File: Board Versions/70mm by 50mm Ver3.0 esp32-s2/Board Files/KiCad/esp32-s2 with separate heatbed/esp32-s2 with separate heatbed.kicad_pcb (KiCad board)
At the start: 2 copper layers, 65.5 x 50 mm, 58 parts, among them IC1 ESP32-S2FN4R2, J1 PJ-037B, J2 USB4520-03-0-A, J3 TB003-500-P02BE, J4 TB003-500-P02BE, J5 Conn_01x03_Male, Q1 PJD25N06A_L2_00001, U1 LD1117S33TR_SOT223, U2 MAX31855KASA, Y1 ECS-400-15-33B-CTN-TR

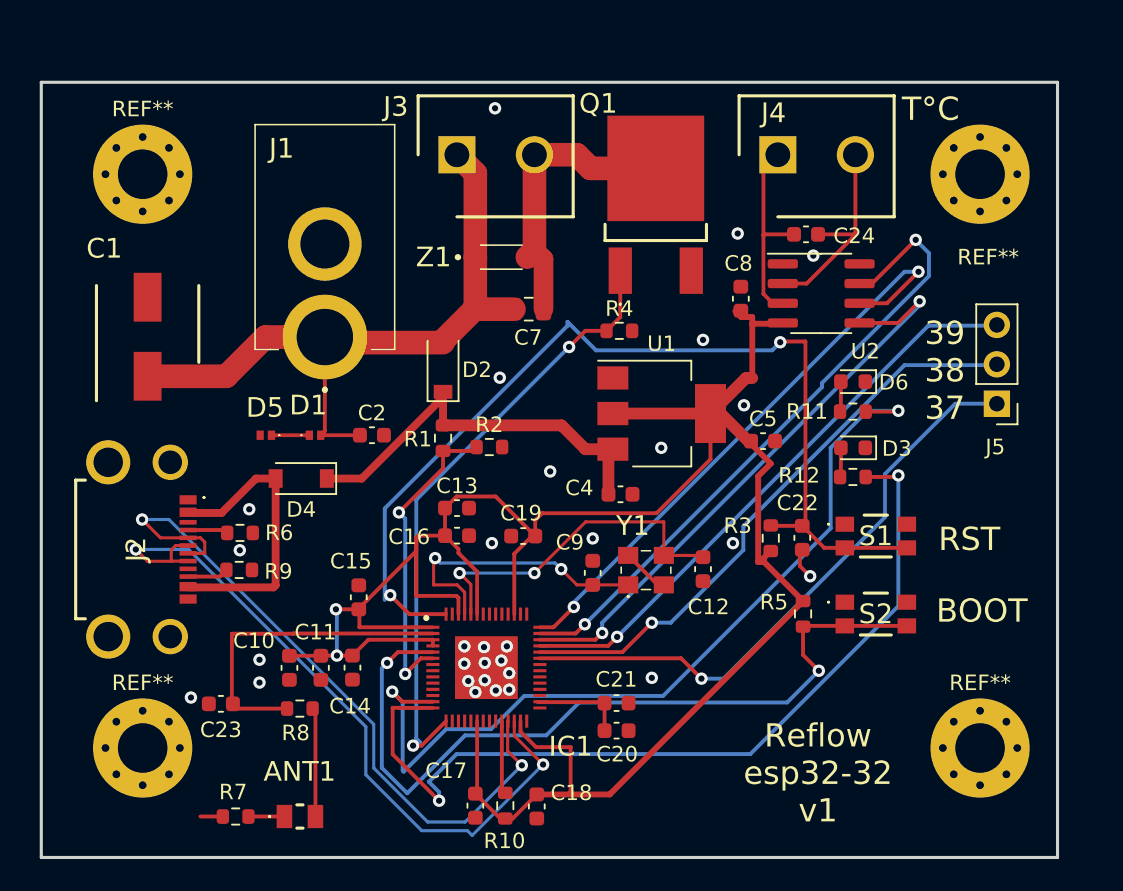
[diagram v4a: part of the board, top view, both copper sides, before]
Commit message: New mounting holes
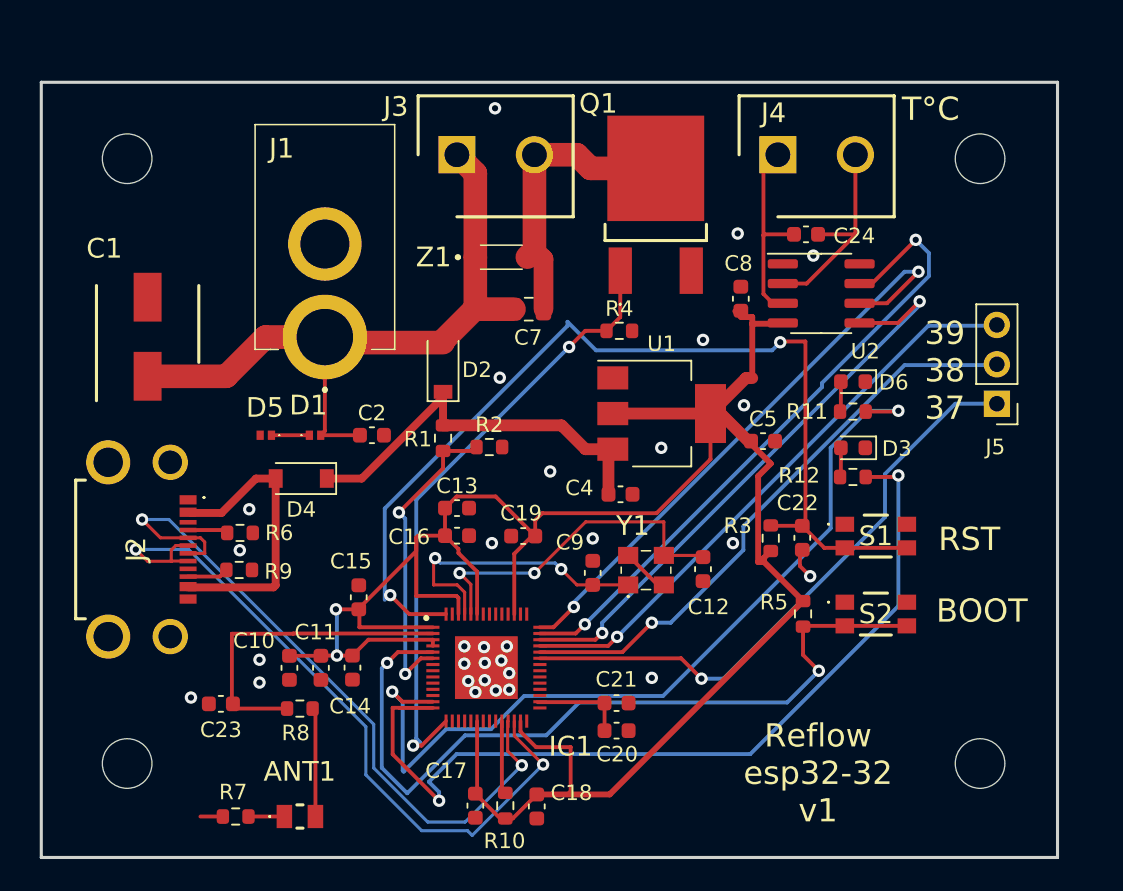
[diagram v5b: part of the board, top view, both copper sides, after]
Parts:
- removed REF** (x4): -, MountingHole:MountingHole_3.2mm_M3_Pad_Via
- added ?: , , F.Cu at (84.8, 17.1)
- added ?: , , F.Cu at (3.01, 62.5)
- added ?: , , F.Cu at (85.3, 61.9)
- added ?: , , F.Cu at (4.72, 14.1)
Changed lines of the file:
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@@
     )
-  )
-  (footprint "MountingHole:MountingHole_3.2mm_M3_Pad_Via" (layer "F.Cu")
-    (at 20 20)
-    (descr "Mounting Hole 3.2mm, M3")
-    (tags "mounting hole 3.2mm m3")
-    (attr exclude_from_pos_files exclude_from_bom)
-    (fp_text reference "REF**" (at 0 -4.2) (layer "F.SilkS")
-      (effects (font (size 1 1) (thickness 0.15)))
-    )
-    (fp_text value "-" (at 0 1.27) (layer "F.Fab")
-      (effects (font (size 1 1) (thickness 0.15)))
-    )
-    (fp_text user "${REFERENCE}" (at 0 0) (layer "F.Fab")
-      (effects (font (size 1 1) (thickness 0.15)))
-    )
-    (fp_circle (center 0 0) (end 3.2 0) (layer "Cmts.User") (width 0.15) (fill none))
-    (fp_circle (center 0 0) (end 3.45 0) (layer "F.CrtYd") (width 0.05) (fill none))
-    (pad "1" thru_hole circle (at 0 0) (size 6.4 6.4) (drill 3.2) (layers *.Cu *.Mask))
-    (pad "1" thru_hole circle (at -2.4 0) (size 0.8 0.8) (drill 0.5) (layers *.Cu *.Mask))
-    (pad "1" thru_hole circle (at 0 -2.4) (size 0.8 0.8) (drill 0.5) (layers *.Cu *.Mask))
-    (pad "1" thru_hole circle (at 0 2.4) (size 0.8 0.8) (drill 0.5) (layers *.Cu *.Mask))
-    (pad "1" thru_hole circle (at 1.697056 1.697056) (size 0.8 0.8) (drill 0.5) (layers *.Cu *.Mask))
-    (pad "1" thru_hole circle (at -1.697056 -1.697056) (size 0.8 0.8) (drill 0.5) (layers *.Cu *.Mask))
-    (pad "1" thru_hole circle (at 1.697056 -1.697056) (size 0.8 0.8) (drill 0.5) (layers *.Cu *.Mask))
-    (pad "1" thru_hole circle (at 2.4 0) (size 0.8 0.8) (drill 0.5) (layers *.Cu *.Mask))
-    (pad "1" thru_hole circle (at -1.697056 1.697056) (size 0.8 0.8) (drill 0.5) (layers *.Cu *.Mask))
   )
   (footprint "library_manager:PJ037B" (layer "F.Cu")
@@
     )
   )
+  (footprint "" (layer "F.Cu")
+    (at 84.7852 17.0688)
+    (fp_text reference "" (at 0 0) (layer "F.SilkS")
+      (effects (font (size 1.27 1.27) (thickness 0.15)))
+    )
+    (fp_text value "" (at 0 0) (layer "F.SilkS")
+      (effects (font (size 1.27 1.27) (thickness 0.15)))
+    )
+    (pad "" np_thru_hole circle (at -10.7852 1.9312) (size 3.2 3.2) (drill 3.2) (layers F&B.Cu *.Mask))
+  )
   (footprint "Resistor_SMD:R_0603_1608Metric" (layer "F.Cu")
     (at 65.7982 35.306 180)
@@
       (rotate (xyz 0 0 0))
     )
-  )
-  (footprint "MountingHole:MountingHole_3.2mm_M3_Pad_Via" (layer "F.Cu")
-    (at 74 20)
-    (descr "Mounting Hole 3.2mm, M3")
-    (tags "mounting hole 3.2mm m3")
-    (attr exclude_from_pos_files exclude_from_bom)
-    (fp_text reference "REF**" (at 0.5236 5.3492) (layer "F.SilkS")
-      (effects (font (size 1 1) (thickness 0.15)))
-    )
-    (fp_text value "-" (at 0 1.27) (layer "F.Fab")
-      (effects (font (size 1 1) (thickness 0.15)))
-    )
-    (fp_text user "${REFERENCE}" (at 0 0) (layer "F.Fab")
-      (effects (font (size 1 1) (thickness 0.15)))
-    )
-    (fp_circle (center 0 0) (end 3.2 0) (layer "Cmts.User") (width 0.15) (fill none))
-    (fp_circle (center 0 0) (end 3.45 0) (layer "F.CrtYd") (width 0.05) (fill none))
-    (pad "1" thru_hole circle (at 0 0) (size 6.4 6.4) (drill 3.2) (layers *.Cu *.Mask))
-    (pad "1" thru_hole circle (at 1.697056 1.697056) (size 0.8 0.8) (drill 0.5) (layers *.Cu *.Mask))
-    (pad "1" thru_hole circle (at 0 -2.4) (size 0.8 0.8) (drill 0.5) (layers *.Cu *.Mask))
-    (pad "1" thru_hole circle (at 0 2.4) (size 0.8 0.8) (drill 0.5) (layers *.Cu *.Mask))
-    (pad "1" thru_hole circle (at -1.697056 1.697056) (size 0.8 0.8) (drill 0.5) (layers *.Cu *.Mask))
-    (pad "1" thru_hole circle (at -2.4 0) (size 0.8 0.8) (drill 0.5) (layers *.Cu *.Mask))
-    (pad "1" thru_hole circle (at -1.697056 -1.697056) (size 0.8 0.8) (drill 0.5) (layers *.Cu *.Mask))
-    (pad "1" thru_hole circle (at 2.4 0) (size 0.8 0.8) (drill 0.5) (layers *.Cu *.Mask))
-    (pad "1" thru_hole circle (at 1.697056 -1.697056) (size 0.8 0.8) (drill 0.5) (layers *.Cu *.Mask))
   )
   (footprint "Capacitor_SMD:C_0603_1608Metric" (layer "F.Cu")
@@
     )
   )
+  (footprint "" (layer "F.Cu")
+    (at 3.0124 62.55)
+    (fp_text reference "" (at 0 0) (layer "F.SilkS")
+      (effects (font (size 1.27 1.27) (thickness 0.15)))
+    )
+    (fp_text value "" (at 0 0) (layer "F.SilkS")
+      (effects (font (size 1.27 1.27) (thickness 0.15)))
+    )
+    (pad "" np_thru_hole circle (at 15.9876 -4.55) (size 3.2 3.2) (drill 3.2) (layers F&B.Cu *.Mask))
+  )
   (footprint "Resistor_SMD:R_0603_1608Metric" (layer "F.Cu")
     (at 42.355 37.592)
@@
       (rotate (xyz 0 0 0))
     )
+  )
+  (footprint "" (layer "F.Cu")
+    (at 85.2932 61.8744)
+    (fp_text reference "" (at 0 0) (layer "F.SilkS")
+      (effects (font (size 1.27 1.27) (thickness 0.15)))
+    )
+    (fp_text value "" (at 0 0) (layer "F.SilkS")
+      (effects (font (size 1.27 1.27) (thickness 0.15)))
+    )
+    (pad "" np_thru_hole circle (at -11.2932 -3.8744) (size 3.2 3.2) (drill 3.2) (layers F&B.Cu *.Mask))
   )
   (footprint "Capacitor_SMD:C_0603_1608Metric" (layer "F.Cu")
@@
     )
   )
-  (footprint "MountingHole:MountingHole_3.2mm_M3_Pad_Via" (layer "F.Cu")
-    (at 74 57)
-    (descr "Mounting Hole 3.2mm, M3")
-    (tags "mounting hole 3.2mm m3")
-    (attr exclude_from_pos_files exclude_from_bom)
-    (fp_text reference "REF**" (at 0 -4.2) (layer "F.SilkS")
-      (effects (font (size 1 1) (thickness 0.15)))
-    )
-    (fp_text value "-" (at 0 1.27) (layer "F.Fab")
-      (effects (font (size 1 1) (thickness 0.15)))
-    )
-    (fp_text user "${REFERENCE}" (at 0 0) (layer "F.Fab")
-      (effects (font (size 1 1) (thickness 0.15)))
-    )
-    (fp_circle (center 0 0) (end 3.2 0) (layer "Cmts.User") (width 0.15) (fill none))
-    (fp_circle (center 0 0) (end 3.45 0) (layer "F.CrtYd") (width 0.05) (fill none))
-    (pad "1" thru_hole circle (at 1.697056 -1.697056) (size 0.8 0.8) (drill 0.5) (layers *.Cu *.Mask))
-    (pad "1" thru_hole circle (at 0 2.4) (size 0.8 0.8) (drill 0.5) (layers *.Cu *.Mask))
-    (pad "1" thru_hole circle (at -1.697056 -1.697056) (size 0.8 0.8) (drill 0.5) (layers *.Cu *.Mask))
-    (pad "1" thru_hole circle (at 2.4 0) (size 0.8 0.8) (drill 0.5) (layers *.Cu *.Mask))
-    (pad "1" thru_hole circle (at 1.697056 1.697056) (size 0.8 0.8) (drill 0.5) (layers *.Cu *.Mask))
-    (pad "1" thru_hole circle (at -2.4 0) (size 0.8 0.8) (drill 0.5) (layers *.Cu *.Mask))
-    (pad "1" thru_hole circle (at 0 -2.4) (size 0.8 0.8) (drill 0.5) (layers *.Cu *.Mask))
-    (pad "1" thru_hole circle (at -1.697056 1.697056) (size 0.8 0.8) (drill 0.5) (layers *.Cu *.Mask))
-    (pad "1" thru_hole circle (at 0 0) (size 6.4 6.4) (drill 3.2) (layers *.Cu *.Mask))
+  (footprint "" (layer "F.Cu")
+    (at 4.7244 14.0716)
+    (fp_text reference "" (at 0 0) (layer "F.SilkS")
+      (effects (font (size 1.27 1.27) (thickness 0.15)))
+    )
+    (fp_text value "" (at 0 0) (layer "F.SilkS")
+      (effects (font (size 1.27 1.27) (thickness 0.15)))
+    )
+    (pad "" np_thru_hole circle (at 14.2756 4.9284) (size 3.2 3.2) (drill 3.2) (layers F&B.Cu *.Mask))
   )
   (footprint "library_manager:ESDL4151MX4T5G" (layer "F.Cu")
@@
     )
   )
-  (footprint "MountingHole:MountingHole_3.2mm_M3_Pad_Via" (layer "F.Cu")
-    (at 20 57)
-    (descr "Mounting Hole 3.2mm, M3")
-    (tags "mounting hole 3.2mm m3")
-    (attr exclude_from_pos_files exclude_from_bom)
-    (fp_text reference "REF**" (at 0 -4.2) (layer "F.SilkS")
-      (effects (font (size 1 1) (thickness 0.15)))
-    )
-    (fp_text value "-" (at 0 1.27) (layer "F.Fab")
-      (effects (font (size 1 1) (thickness 0.15)))
-    )
-    (fp_text user "${REFERENCE}" (at 0 0) (layer "F.Fab")
-      (effects (font (size 1 1) (thickness 0.15)))
-    )
-    (fp_circle (center 0 0) (end 3.2 0) (layer "Cmts.User") (width 0.15) (fill none))
-    (fp_circle (center 0 0) (end 3.45 0) (layer "F.CrtYd") (width 0.05) (fill none))
-    (pad "1" thru_hole circle (at 0 2.4) (size 0.8 0.8) (drill 0.5) (layers *.Cu *.Mask))
-    (pad "1" thru_hole circle (at -1.697056 1.697056) (size 0.8 0.8) (drill 0.5) (layers *.Cu *.Mask))
-    (pad "1" thru_hole circle (at -1.697056 -1.697056) (size 0.8 0.8) (drill 0.5) (layers *.Cu *.Mask))
-    (pad "1" thru_hole circle (at 1.697056 -1.697056) (size 0.8 0.8) (drill 0.5) (layers *.Cu *.Mask))
-    (pad "1" thru_hole circle (at -2.4 0) (size 0.8 0.8) (drill 0.5) (layers *.Cu *.Mask))
-    (pad "1" thru_hole circle (at 0 0) (size 6.4 6.4) (drill 3.2) (layers *.Cu *.Mask))
-    (pad "1" thru_hole circle (at 2.4 0) (size 0.8 0.8) (drill 0.5) (layers *.Cu *.Mask))
-    (pad "1" thru_hole circle (at 1.697056 1.697056) (size 0.8 0.8) (drill 0.5) (layers *.Cu *.Mask))
-    (pad "1" thru_hole circle (at 0 -2.4) (size 0.8 0.8) (drill 0.5) (layers *.Cu *.Mask))
-  )
   (footprint "Diode_SMD:D_SOD-123" (layer "F.Cu")

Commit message: Spacing
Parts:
- moved C24 2.16 mm to (64.6, 25.1)
- moved U2 1.07 mm to (63.7, 28.8)
- moved Z1 0.41 mm to (43.1, 25.8)
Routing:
- net Net-(U2-Pad3): track 12.9 -> 16.0 mm
- net EN: track 64.6 -> 63.0 mm
- net Net-(J4-Pad2): track 13.6 -> 12.0 mm
- net tempSO: track 42.3 -> 43.1 mm
- net Net-(C7-Pad2): track 19.0 -> 19.5 mm
- net GND: vias 30 -> 35

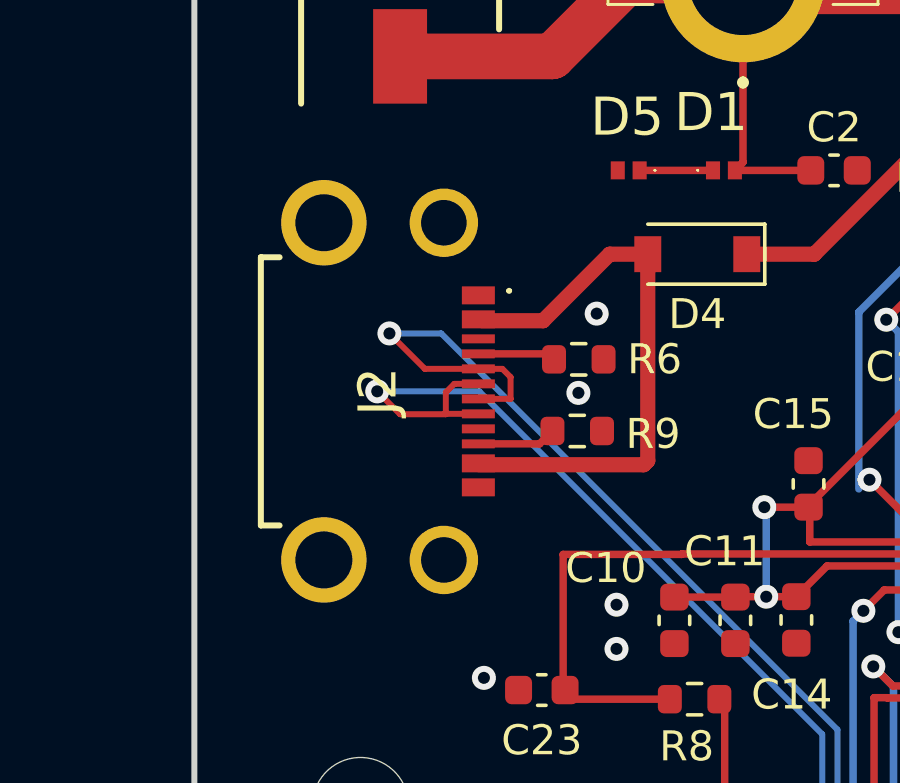
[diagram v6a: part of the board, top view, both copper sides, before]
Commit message: Replace wrong USB-C with a correct one
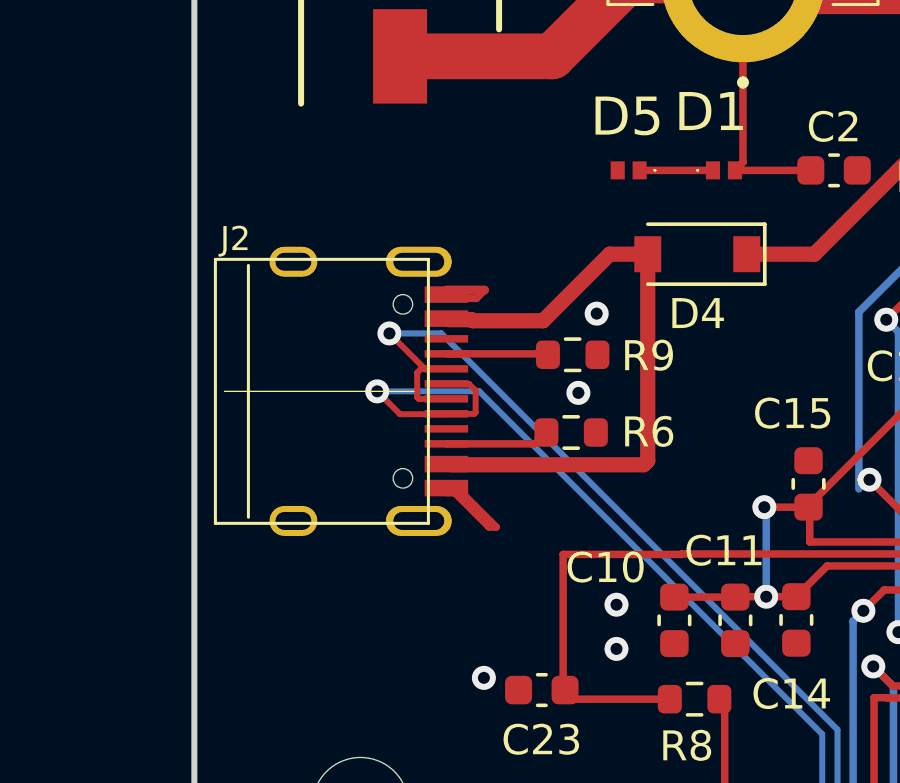
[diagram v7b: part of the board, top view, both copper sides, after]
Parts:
- J2: value USB4520-03-0-A -> USB_C_Receptacle_USB2.0; footprint library_manager:USB4520030A -> library_manager:TYPE-C-31-M-12
- moved R9 2.54 mm to (26.1, 43.0), turned to 0 degrees
- moved J2 2.54 mm to (16.8, 44.2)
- moved R6 2.45 mm to (26.0, 45.6)
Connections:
- J2 pad A5: Net-(J2-PadA5) -> Net-(R9-Pad1)
- J2 pad B5: Net-(J2-PadB5) -> Net-(R6-Pad2)
- R6 pad 2: Net-(J2-PadA5) -> Net-(R6-Pad2)
- R9 pad 1: GND -> Net-(R9-Pad1)
- R9 pad 2: Net-(J2-PadB5) -> GND
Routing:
- net GND: track 6.70 -> 13.7 mm
- net Net-(R6-Pad2): track 0.00 -> 3.49 mm
- net Net-(R9-Pad1): track 0.00 -> 3.40 mm
- net Net-(J2-PadB5): track 2.65 -> 0.00 mm
- net Net-(J2-PadA5): track 2.60 -> 0.00 mm
- net Net-(D4-Pad2): track 19.0 -> 21.1 mm
- net D-: track 45.4 -> 43.5 mm
